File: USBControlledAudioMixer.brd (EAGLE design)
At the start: 42.5 x 40 mm, 36 parts, among them IC1 TDA7448, IC2 TS912, IC3 MEGA8-AI, J1 MOLEX 47346-0001, J2 AVR_SPI_PRG_6NS

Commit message: Minor update (sorry for nonsense commit message)
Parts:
- removed D2: BZX84CSMD, diode:TO236
- removed LED6, LED7, LED8: (no value), led:CHIPLED-0603-TTW
- added D3: (no value), diode:SOT23
- added IC4: OPA344N-SOT23, linear:SOT23-5
- added JP1: (no value), pinhead:1X04/90
- added L1: (no value), rcl:L3225M
- added R10, R11, R6, R7, R8, R9: (no value), rcl:R0603
- added R12: 470, rcl:R0603
- added R13, R14: 62, rcl:R0603
- added R15: 1k5, rcl:R0603
- added U$1: 470, Simplex-rlc:YC164
- C1, C2: value 22p -> 12p; device rcl:C0805K -> rcl:C0603
- C10, C11, C6, C7, C8, C9: value 22p -> 470n; device rcl:C0805K -> rcl:C0603
- C3: device rcl:C0805K -> rcl:C0603
- C4: device rcl:A/3216-18W -> rcl:SMC_A
- D1: value BZX84CSMD -> (none); device diode:TO236 -> diode:SOD123
- Q1: value (none) -> 16MHz; device crystal:HC49UP -> nonolith:CRYSTAL_3.2X2.5
- R3: device rcl:R0805 -> rcl:R0603
- moved C6 109.3 mm to (-23.5, -40.0), flipped to the top
- moved C7 109.1 mm to (-23.5, -44.8), flipped to the top
- moved C8 109.0 mm to (-23.5, -49.5), flipped to the top
- moved C9 108.8 mm to (-23.5, -54.2), flipped to the top
- moved C10 108.6 mm to (-23.5, -59.0), flipped to the top
- moved C11 108.4 mm to (-23.5, -63.8), flipped to the top
- moved C5 57.3 mm to (32.9, 15.7), flipped to the top
- moved R1 52.9 mm to (18.4, -15.6), flipped to the top
- moved C2 51.7 mm to (29.6, 15.1), flipped to the top, turned to 180 degrees
- moved R4 51.5 mm to (35.6, 16.5), flipped to the top
- moved C1 50.5 mm to (29.8, 12.6), flipped to the top, turned to 180 degrees
- moved C3 49.0 mm to (27.0, 9.61), flipped to the top, turned to 0 degrees
- moved IC3 40.0 mm to (19.9, 19.7), flipped to the top, turned to 90 degrees
- moved J2 38.8 mm to (28.4, 27.7)
- moved Q1 37.9 mm to (26.0, 13.9), flipped to the top, turned to 90 degrees
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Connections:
- new net LED1: IC3.10, LED1.A@1
- new net LED2: IC3.11, LED2.A@1
- new net LED3: IC3.12, LED3.A@1
- new net LED4: IC3.13, LED4.A@1
- new net LED5: IC3.14, LED5.A@1
- new net N$11: D3.2, JP1.2, R13.2, R15.2
- new net N$13: D3.1, JP1.3, R14.2
- new net N$5: LED1.C@1, U$1.8
- new net N$6: LED2.C@1, U$1.7
- new net N$7: LED3.C@1, U$1.6
- new net N$8: LED4.C@1, U$1.5
- new net N$9: LED5.C@1, R12.2
- net +5V: now also JP1.1, R15.1
- net D+: now also IC3.32, R14.1; no longer IC3.24
- net D-: now also IC3.2, R13.1; no longer IC3.23
- net GND: now also D3.3, JP1.4, R12.1, U$1.1, U$1.2, U$1.3, U$1.4
- net V+: now also IC4.5
- net V-: now also IC4.2

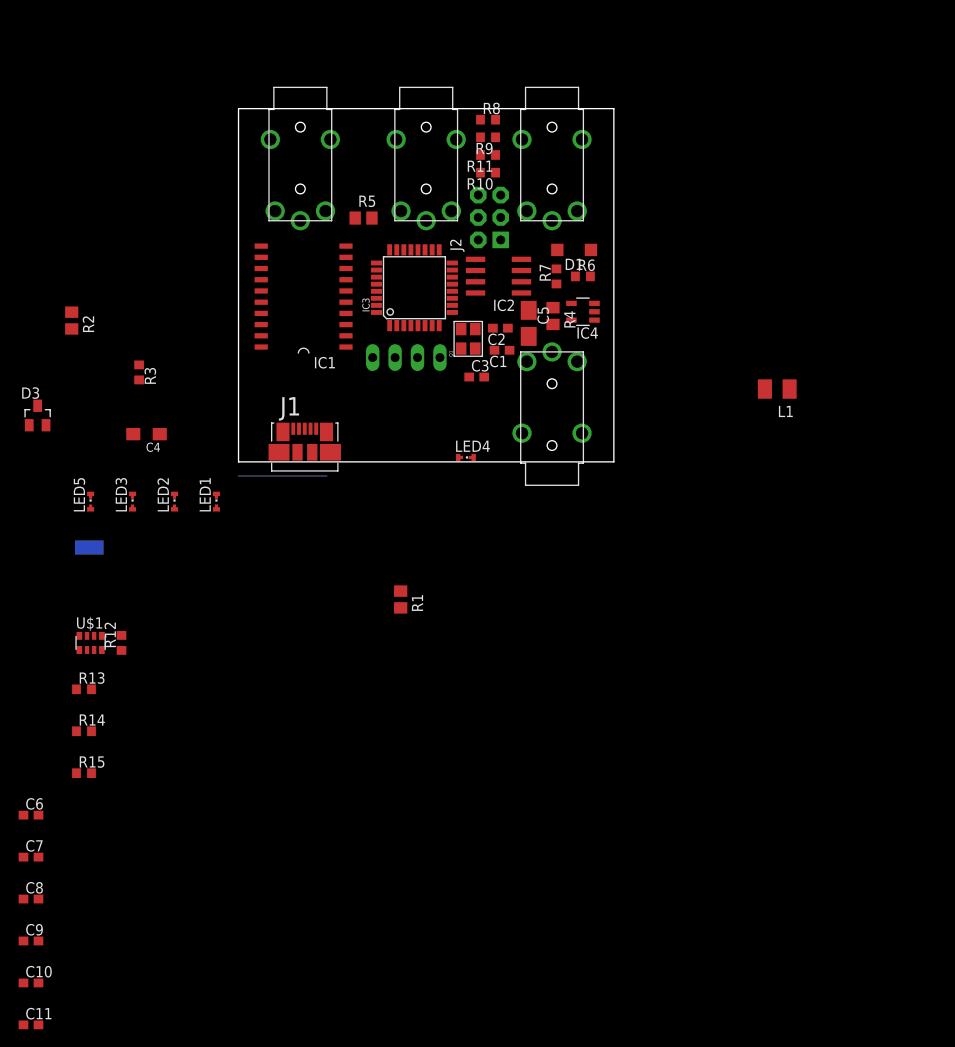
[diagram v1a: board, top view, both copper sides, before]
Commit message: Added LEDs an basic wiring
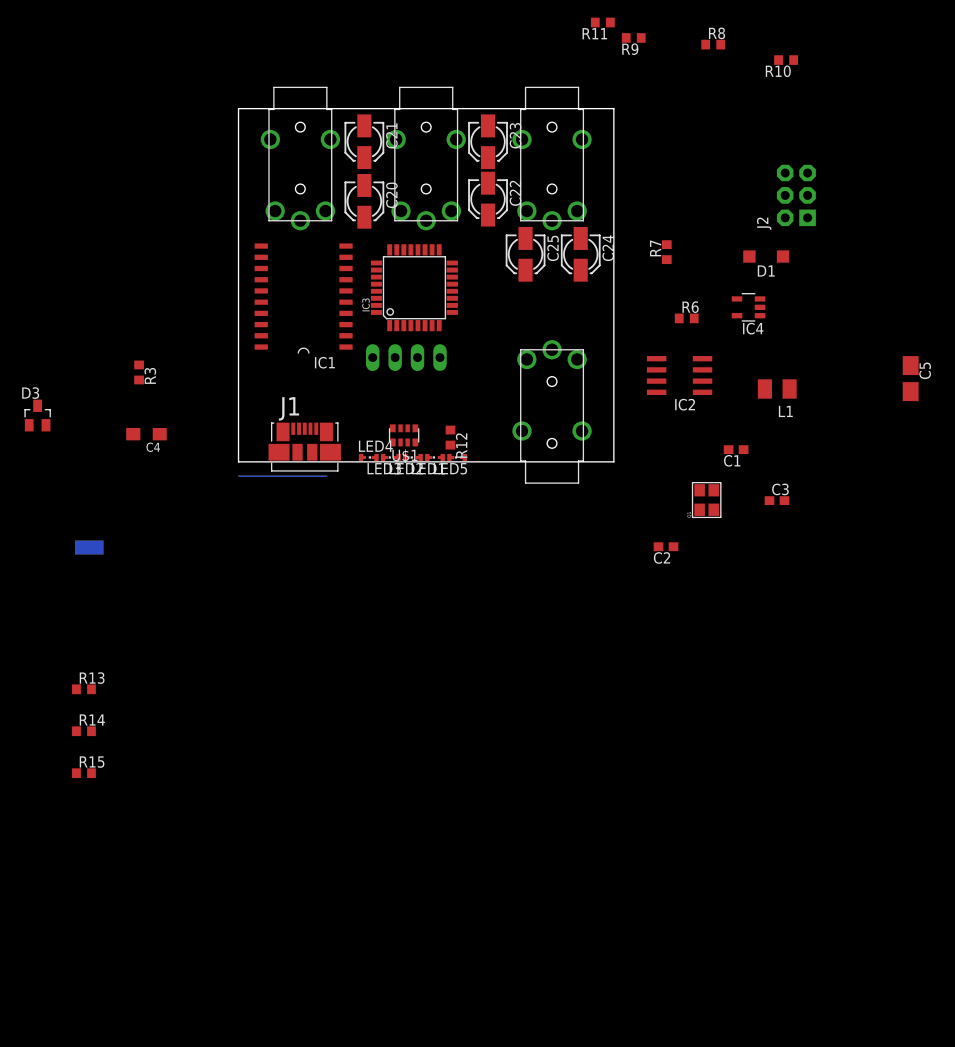
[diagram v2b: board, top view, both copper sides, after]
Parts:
- removed C10, C11, C6, C7, C8, C9: 470n, rcl:C0603
- removed R1, R2: 68, rcl:R0805
- removed R4: 10k, rcl:R0805
- removed R5: 2k2, rcl:R0805
- removed U$2: FC68125, FC68125:FC68125
- added C20, C21, C22, C23, C24, C25: 10u, rcl:153CLV-0405
- added IN1: FC68125, FC68125:FC68125
- moved R12 43.9 mm to (24.0, 2.75), turned to 270 degrees
- moved C5 43.7 mm to (76.1, 9.43)
- moved U$1 42.6 mm to (18.8, 3.00), turned to 180 degrees
- moved LED5 41.8 mm to (24.8, 0.50), turned to 90 degrees
- moved U$5 39.5 mm to (35.5, 6.34), turned to 180 degrees
- moved C3 36.8 mm to (61.0, -4.39)
- moved R10 36.1 mm to (62.0, 45.5)
- moved J2 34.8 mm to (63.2, 30.2)
- moved Q1 32.6 mm to (53.0, -4.32)
- moved C2 31.1 mm to (48.4, -9.61)
- moved LED3 29.7 mm to (17.2, 0.50), turned to 90 degrees
- moved C1 28.8 mm to (56.3, 1.39)
- moved LED2 27.5 mm to (19.8, 0.50), turned to 90 degrees
- moved R8 26.9 mm to (53.8, 47.2)
- moved LED1 25.2 mm to (22.2, 0.50), turned to 90 degrees
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- renumbered U$3 to IN3, U$4 to IN2
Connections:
- net OUT1 renamed OUT_1_L
- net OUT2 renamed OUT_1_R
- net OUT3 renamed OUT_2_L
- net OUT4 renamed OUT_2_R
- net OUT5 renamed OUT_3_L
- net OUT6 renamed OUT_3_R
- removed net IN1: IC1.2
- removed net IN2: IC1.19
- removed net IN3: IC1.3
- removed net IN4: IC1.18
- removed net IN5: IC1.4
- removed net IN6: IC1.17
- new net IN_1_L: C20.+, IC1.2
- new net IN_1_R: C21.+, IC1.19
- new net IN_2_L: C22.+, IC1.3
- new net IN_2_R: C23.+, IC1.18
- new net IN_3_L: C24.+, IC1.4
- new net IN_3_R: C25.+, IC1.17
- new net N$10: C24.-, IN3.6
- new net N$12: C25.-, IN3.3, IN3.3A
- new net N$14: C22.-, IN2.6
- new net N$15: C23.-, IN2.3, IN2.3A
- new net N$16: C20.-, IN1.6
- new net N$17: C21.-, IN1.3, IN1.3A
- new net N$18: IC3.23
- new net N$19: IC3.24
- new net N$20: IC3.25
- net GND: now also IN1.1, IN1.2, IN2.1, IN2.2, IN3.1, IN3.2

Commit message: Pre-final version without proper board layout
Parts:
- removed D1: (no value), diode:SOD123
- removed IC4: OPA344N-SOT23, linear:SOT23-5
- removed JP1: (no value), pinhead:1X04/90
- removed L1: (no value), rcl:L3225M
- removed R10, R11, R6, R7, R8, R9: (no value), rcl:R0603
- added C10, C9: 10u, rcl:153CLV-0405
- added C11: 100n, rcl:C0603
- added C6: 10µ, rcl:C0805
- added C7: 2.2µ, rcl:C0603
- added C8: 330p, rcl:C0603
- added D2: (no value), adafruit:SOD-123
- added JP2: (no value), pinhead:1X03/90
- added L2: (no value), SparkFun:1007
- added R1, R16, R17, R5: 1M, rcl:R0603
- added R18, R19, R20: 1k, rcl:R0603
- added R2: 13.3k, rcl:R0603
- added R4: 84.5k, rcl:R0603
- added U1: LMR62014, projectLibrary:SOT-23
- J1: value MOLEX 47346-0001 -> (none)
- moved C5 73.8 mm to (2.36, 9.68)
- moved R15 47.8 mm to (4.75, 7.00), turned to 270 degrees
- moved R14 46.5 mm to (11.0, 6.25), turned to 180 degrees
- moved R13 44.4 mm to (11.0, 8.25), turned to 180 degrees
- moved C3 42.2 mm to (23.7, 15.4)
- moved C1 34.5 mm to (22.6, 8.91), turned to 90 degrees
- moved Q1 33.8 mm to (23.7, 12.5), turned to 0 degrees
- moved D3 30.3 mm to (7.50, 7.25)
- moved C2 29.9 mm to (24.9, 8.85), turned to 90 degrees
- moved R3 25.9 mm to (14.0, 15.6), turned to 90 degrees
- moved C4 19.3 mm to (7.17, 11.1), turned to 0 degrees
- moved IC2 19.2 mm to (32.5, 17.9)
- moved J2 16.4 mm to (54.2, 16.4)
- moved C24 6.76 mm to (38.8, 16.7)
- moved C25 6.52 mm to (39.0, 24.0)
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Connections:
- removed net OUT_1_L: IC1.7
- removed net OUT_1_R: IC1.14
- removed net OUT_2_L: IC1.6
- removed net OUT_2_R: IC1.15
- removed net OUT_3_L: IC1.5
- removed net OUT_3_R: IC1.16
- removed net V+: IC2.8, IC4.5
- removed net V-: IC2.4, IC4.2
- new net +9V: C6.1, C8.2, D2.C, R4.1
- new net N$21: R1.2, U1.4
- new net N$22: D2.A, L2.2, U1.1
- new net N$23: C9.-, U$5.6
- new net N$24: C9.+, IC2.1, IC2.2
- new net N$25: C8.1, R2.2, R4.2, U1.3
- new net N$26: C10.-, U$5.3, U$5.3A
- new net N$27: IC2.5
- new net OUT_L: IC1.5, IC1.6, IC1.7, IC2.3
- new net OUT_R: C10.+, IC1.14, IC1.15, IC1.16, IC2.6, IC2.7
- new net TOUCH_RCV_+: IC3.23, R19.1
- new net TOUCH_RCV_-: IC3.24, R18.1
- new net TOUCH_RCV_CHAN: IC3.25, R20.1
- new net TOUCH_SEND_+: IC3.26, R16.1
- new net TOUCH_SEND_-: IC3.1, R5.1
- new net TOUCH_SEND_CHAN: IC3.9, R17.1
- net +5V: now also C11.1, C7.1, IC2.8, J1.1, L2.1, R1.1, U1.5; no longer JP1.1
- net GND: now also C11.2, C6.2, C7.2, IC2.4, J1.5, R2.1, U$5.1, U1.2; no longer JP1.4
- net N$11: now also D3.1, J1.2; no longer D3.2, JP1.2
- net N$13: now also D3.2, J1.3; no longer D3.1, JP1.3
- net N$18: now also JP2.1, R18.2, R5.2; no longer IC3.23
- net N$19: now also JP2.2, R16.2, R19.2; no longer IC3.24
- net N$20: now also JP2.3, R17.2, R20.2; no longer IC3.25
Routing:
- added copper zone on layer 1, net GND

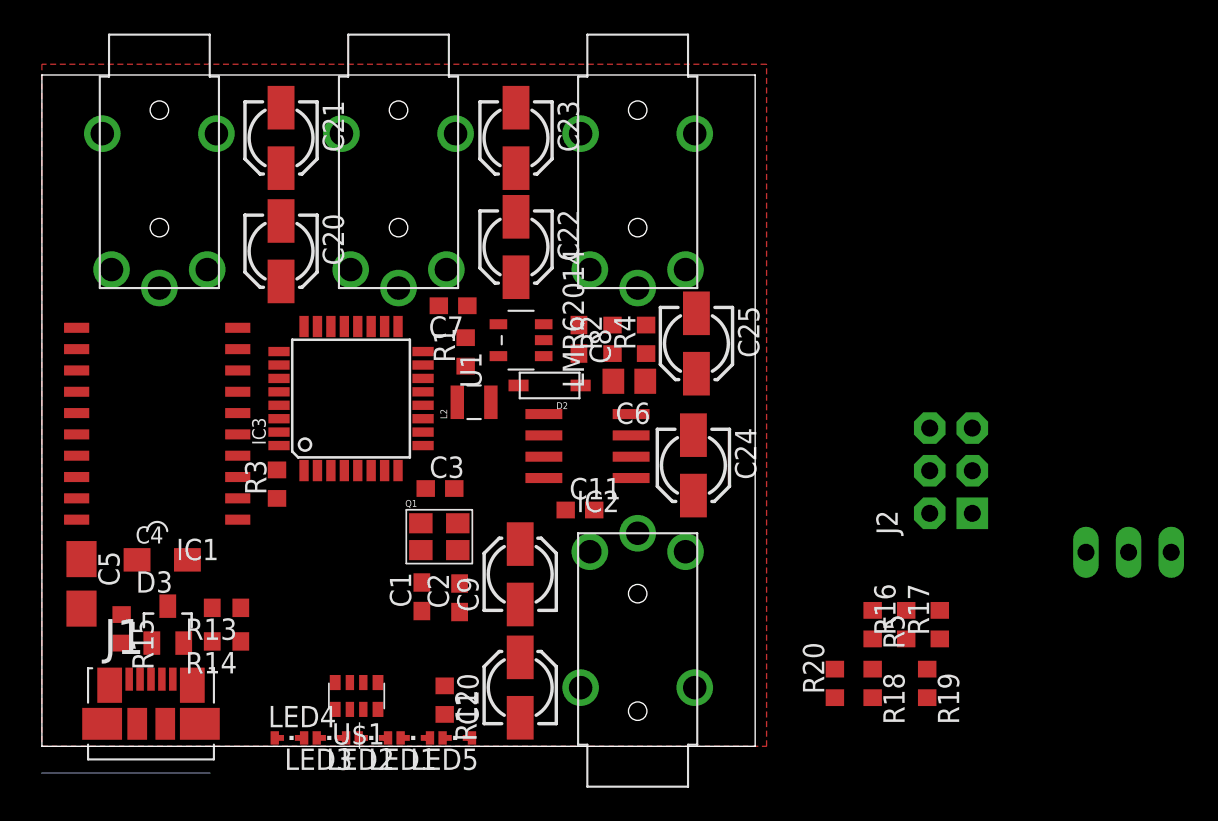
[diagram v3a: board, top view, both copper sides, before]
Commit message: Routing done, silkscreen adjustments missing
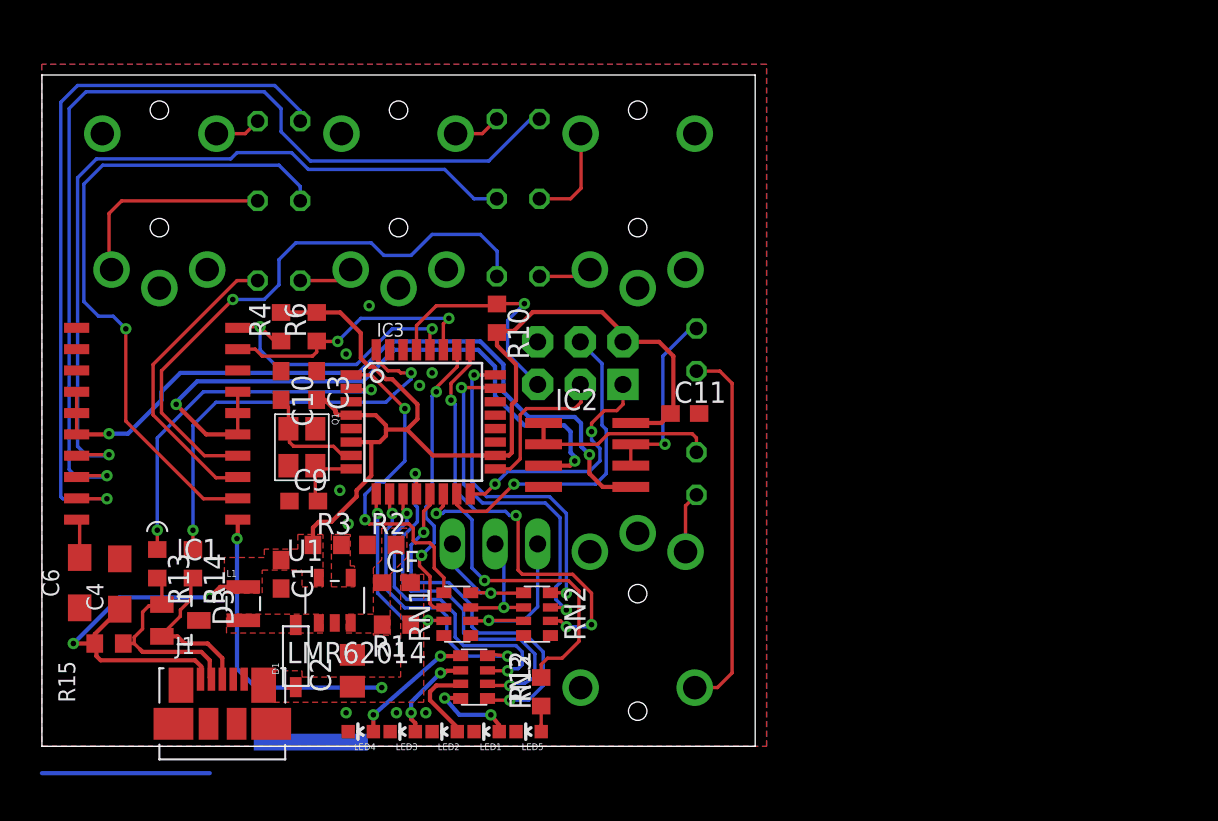
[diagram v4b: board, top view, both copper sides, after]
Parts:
- removed C5: 10u, rcl:A/3216-18W
- removed C7: 2.2µ, rcl:C0603
- removed C8: 330p, rcl:C0603
- removed D2: (no value), adafruit:SOD-123
- removed L2: (no value), SparkFun:1007
- removed R16, R17, R5: 1M, rcl:R0603
- removed R18, R19, R20: 1k, rcl:R0603
- removed U$1: 470, Simplex-rlc:YC164
- added C26, C27: 470n, rcl:C025-050X050
- added CF: 330p, rcl:C0603
- added D1: (no value), adafruit:SOD-123
- added L1: (no value), SparkFun:1007
- added R10: 10k, rcl:R0603
- added R6: 4k7, rcl:R0603
- added RN1: 1M, Simplex-rlc:YC164
- added RN2: 1k, Simplex-rlc:YC164
- added RN3: 470, Simplex-rlc:YC164
- C1: value 12p -> 2.2µ
- C10, C9: value 10u -> 12p; device rcl:153CLV-0405 -> rcl:C0603
- C2: value 12p -> 10µ; device rcl:C0603 -> rcl:C0805
- C20, C21, C22, C23, C24, C25: value 10u -> 470n; device rcl:153CLV-0405 -> rcl:C025-050X050
- C6: value 10µ -> 10u; device rcl:C0805 -> rcl:SMC_A
- LED1, LED2, LED3, LED4, LED5: device led:CHIPLED-0603-TTW -> SparkFun:LED-0603
- R1: value 1M -> 84.5k
- R3: value 10k -> 1M
- R4: value 84.5k -> 4k7
- moved JP2 37.8 mm to (27.0, 8.25)
- moved C6 34.9 mm to (2.25, 9.75), turned to 270 degrees
- moved J2 23.0 mm to (32.1, 22.8), flipped to the bottom, turned to 0 degrees
- moved C10 23.0 mm to (14.2, 21.5), turned to 270 degrees
- moved R4 21.8 mm to (14.2, 25.0)
- moved U1 19.0 mm to (17.5, 8.75), turned to 0 degrees
- moved R2 18.4 mm to (20.2, 12.0), turned to 0 degrees
- moved R1 16.8 mm to (21.1, 7.25), turned to 180 degrees
- moved C24 15.4 mm to (28.4, 28.0), flipped to the bottom, turned to 0 degrees
- moved C22 14.3 mm to (14.1, 27.8), flipped to the bottom, turned to 0 degrees
- moved C25 13.7 mm to (28.4, 32.6), flipped to the bottom, turned to 0 degrees
- moved C9 13.6 mm to (15.6, 14.6), turned to 0 degrees
- moved Q1 9.77 mm to (15.5, 17.8), turned to 270 degrees
- moved C3 9.57 mm to (16.4, 21.5), turned to 270 degrees
- moved C1 8.50 mm to (14.2, 10.2), turned to 270 degrees
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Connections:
- removed net AVCC: IC3.18
- removed net N$21: R1.2, U1.4
- removed net N$22: D2.A, L2.2, U1.1
- removed net N$25: C8.1, R2.2, R4.2, U1.3
- removed net N$27: IC2.5
- new net FB: CF.1, R1.2, R2.2, U1.3
- new net N$100: C27.1, IC2.6, IC2.7
- new net SHDN: R3.2, U1.4
- new net SW: D1.A, L1.2, U1.1
- net +5V: now also C1.1, IC3.18, L1.1, R10.2, R3.1, R4.2, R6.2; no longer C7.1, IC1.1, L2.1, R1.1, R3.2
- net +9V: now also C2.1, CF.2, D1.C, IC1.1, R1.1; no longer C6.1, C8.2, D2.C, R4.1
- net GND: now also C1.2, C10.1, C2.2, C6.-, C9.1, LED1.C, LED2.C, LED3.C, LED4.C, LED5.C; no longer C1.1, C2.1, C5.-, C6.2, C7.2, R12.1, U$1.1, U$1.2, U$1.3, U$1.4
- net IN_1_L: now also C20.2; no longer C20.+
- net IN_1_R: now also C21.2; no longer C21.+
- net IN_2_L: now also C22.2; no longer C22.+
- net IN_2_R: now also C23.2; no longer C23.+
- net IN_3_L: now also C24.2; no longer C24.+
- net IN_3_R: now also C25.2; no longer C25.+
- net LED1: now also IC3.13, RN3.1; no longer IC3.10, LED1.A@1
- net LED2: now also IC3.12, RN3.2; no longer IC3.11, LED2.A@1
- net LED3: now also IC3.11, RN3.3; no longer IC3.12, LED3.A@1
- net LED4: now also IC3.10, RN3.4; no longer IC3.13, LED4.A@1
- net LED5: now also R12.2; no longer LED5.A@1
- net N$1: now also C6.+; no longer C5.+
- net N$10: now also C24.1; no longer C24.-
- net N$12: now also C25.1; no longer C25.-
- net N$14: now also C22.1; no longer C22.-
- net N$15: now also C23.1; no longer C23.-
- net N$16: now also C20.1; no longer C20.-
- net N$17: now also C21.1; no longer C21.-
- net N$18: now also RN1.4, RN2.1; no longer R18.2, R5.2
- net N$19: now also RN1.3, RN2.2; no longer R16.2, R19.2
- net N$2: now also C9.2; no longer C2.2
- net N$20: now also RN1.2, RN2.3; no longer R17.2, R20.2
- net N$23: now also C26.2; no longer C9.-
- net N$24: now also C26.1; no longer C9.+
- net N$26: now also C27.2; no longer C10.-
- net N$3: now also C10.2; no longer C1.2
- net N$5: now also LED1.A, RN3.8; no longer LED1.C@1, U$1.8
- net N$6: now also LED2.A, RN3.7; no longer LED2.C@1, U$1.7
- net N$7: now also LED3.A, RN3.6; no longer LED3.C@1, U$1.6
- net N$8: now also LED4.A, RN3.5; no longer LED4.C@1, U$1.5
- net N$9: now also LED5.A, R12.1; no longer LED5.C@1, R12.2
- net OUT_R: now also IC2.5; no longer C10.+, IC2.6, IC2.7
- net RESET: now also R10.1; no longer R3.1
- net SCL: now also R4.1
- net SDA: now also R6.1
- net TOUCH_RCV_+: now also RN2.7; no longer R19.1
- net TOUCH_RCV_-: now also RN2.8; no longer R18.1
- net TOUCH_RCV_CHAN: now also RN2.6; no longer R20.1
- net TOUCH_SEND_+: now also RN1.6; no longer R16.1
- net TOUCH_SEND_-: now also RN1.5; no longer R5.1
- net TOUCH_SEND_CHAN: now also RN1.7; no longer R17.1
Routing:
- net +5V: track 0.00 -> 86.7 mm, vias 0 -> 2
- net IN_2_R: track 0.00 -> 57.8 mm, vias 0 -> 1
- net IN_3_R: track 0.00 -> 46.8 mm, vias 0 -> 1
- net OUT_R: track 0.00 -> 44.2 mm, vias 0 -> 2
- net IN_1_R: track 0.00 -> 44.0 mm, vias 0 -> 1
- net IN_1_L: track 0.00 -> 39.0 mm, vias 0 -> 1
- net OUT_L: track 0.00 -> 38.7 mm, vias 0 -> 2
- net IN_3_L: track 0.00 -> 34.9 mm, vias 0 -> 1
- net TOUCH_RCV_CHAN: track 0.00 -> 26.0 mm, vias 0 -> 4
- net D+: track 0.00 -> 24.8 mm, vias 0 -> 2
- net LED2: track 0.00 -> 23.0 mm, vias 0 -> 2
- net N$26: track 0.00 -> 22.3 mm
- net D-: track 0.00 -> 21.8 mm, vias 0 -> 2
- net LED1: track 0.00 -> 21.7 mm, vias 0 -> 2
- net TOUCH_RCV_+: track 0.00 -> 21.3 mm, vias 0 -> 2
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- added copper zone on layer 1, net +5V
- added copper zone on layer 1, net +9V
- added copper zone on layer 1, net FB
- added copper zone on layer 16, net GND
- added copper zone on layer 1, net SHDN
- added copper zone on layer 1, net SW
